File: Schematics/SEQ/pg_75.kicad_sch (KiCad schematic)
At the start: 16 parts, among them U7601 93S48, U7602 93S48, U7603 93S48, U7604 93S48, U7605 F244, U7606 F04, U7607 F02, U7608 F00, U7609 F02, U7610 F51, U7611 F74, U7612 F74, U7613 F74, U7614 F04, U7615 F02, U7616 F51

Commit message: Much work on SEQ
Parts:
- removed U7612, U7613: F74, symbol r1000:F74
- U7611: value F74 -> F175; symbol r1000:F74 -> r1000:F175; Location G36 -> x99
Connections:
- net LEX_ADR.WCS0: now also U7611.12 (D2)
- net MAYBE_DISPATCH~: now also U7611.3 (Q0~); no longer U7611.6 (Q_)
- net PREDECODE.CLK~: now also U7611.9 (CLK); no longer U7611.3 (CLK)
- net PU: no longer U7611.4 (PR_), U7616.1 (A1), U7616.4 (B1)
- net RES_ADR.SEL1: now also U7611.15 (Q3)
- net at U7609.3 (Q): now also U7611.13 (D3)
- net at U7610.7 (Q): now also U7611.4 (D0); no longer U7611.2 (D)
- net at U7616.2 (A2): now also U7611.2 (Q0), U7616.1 (A1); no longer U7611.5 (Q)
- net at U7615.1 (D0), U7616.5 (B2), U7616.6 (B3): now also U7611.10 (Q2), U7616.4 (B1)
- no-connect marks 6 -> 9
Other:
- moved on the sheet: U7608, U7609, U7610, U7614, U7615, U7616

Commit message: KiCad 6
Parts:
- U7601, U7602, U7603, U7604: value 93S48 -> (none)
- U7605: value F244 -> (none)
- U7606, U7614: value F04 -> (none)
- U7607, U7609, U7615: value F02 -> (none)
- U7608: value F00 -> (none)
- U7610, U7616: value F51 -> (none)
- U7611: value F175 -> (none)

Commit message: Recover from KiCad-6 munging
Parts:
- U7601, U7602, U7603, U7604: value (none) -> 93S48
- U7605: value (none) -> F244
- U7606, U7614: value (none) -> F04
- U7607, U7609, U7615: value (none) -> F02
- U7608: value (none) -> F00
- U7610, U7616: value (none) -> F51
- U7611: value (none) -> F175

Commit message: Snapshot
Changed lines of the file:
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@@
   (bus (pts (xy 353.06 345.44) (xy 353.06 350.52) ) )
   (bus (pts (xy 353.06 350.52) (xy 353.06 355.6) ) )
-  (bus (pts (xy 353.06 355.6) (xy 353.06 360.68) ) )
   (wire (pts (xy 124.46 193.04) (xy 124.46 215.9) ) )
   (wire (pts (xy 124.46 215.9) (xy 134.62 215.9) ) )

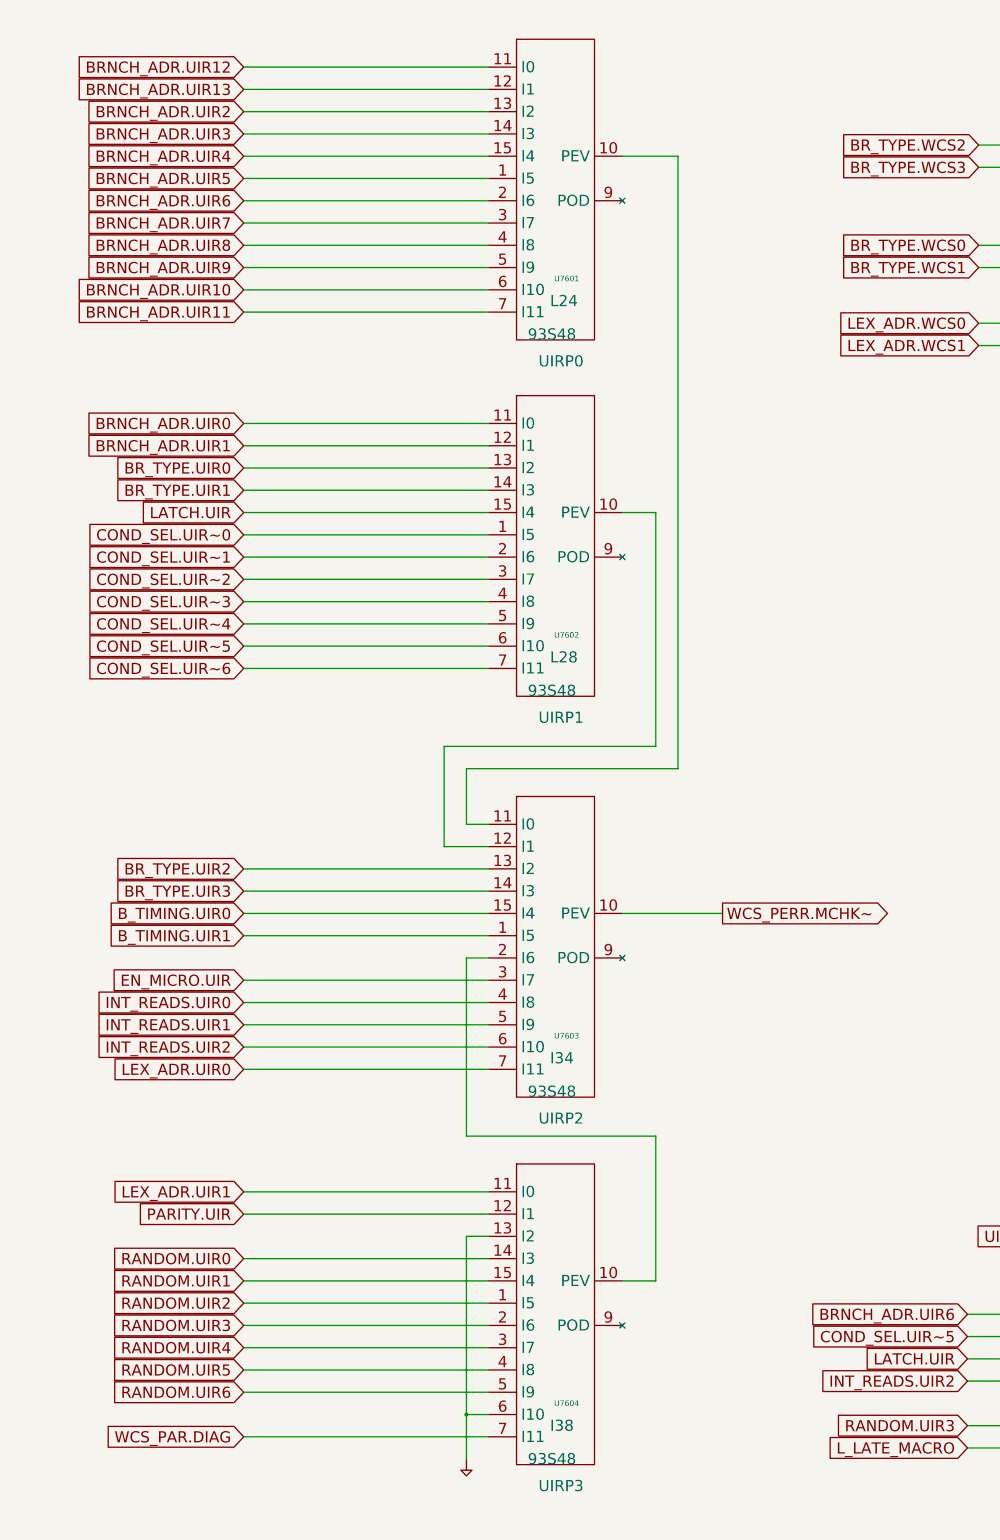
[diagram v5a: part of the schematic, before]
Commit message: Megacom WCS + parity
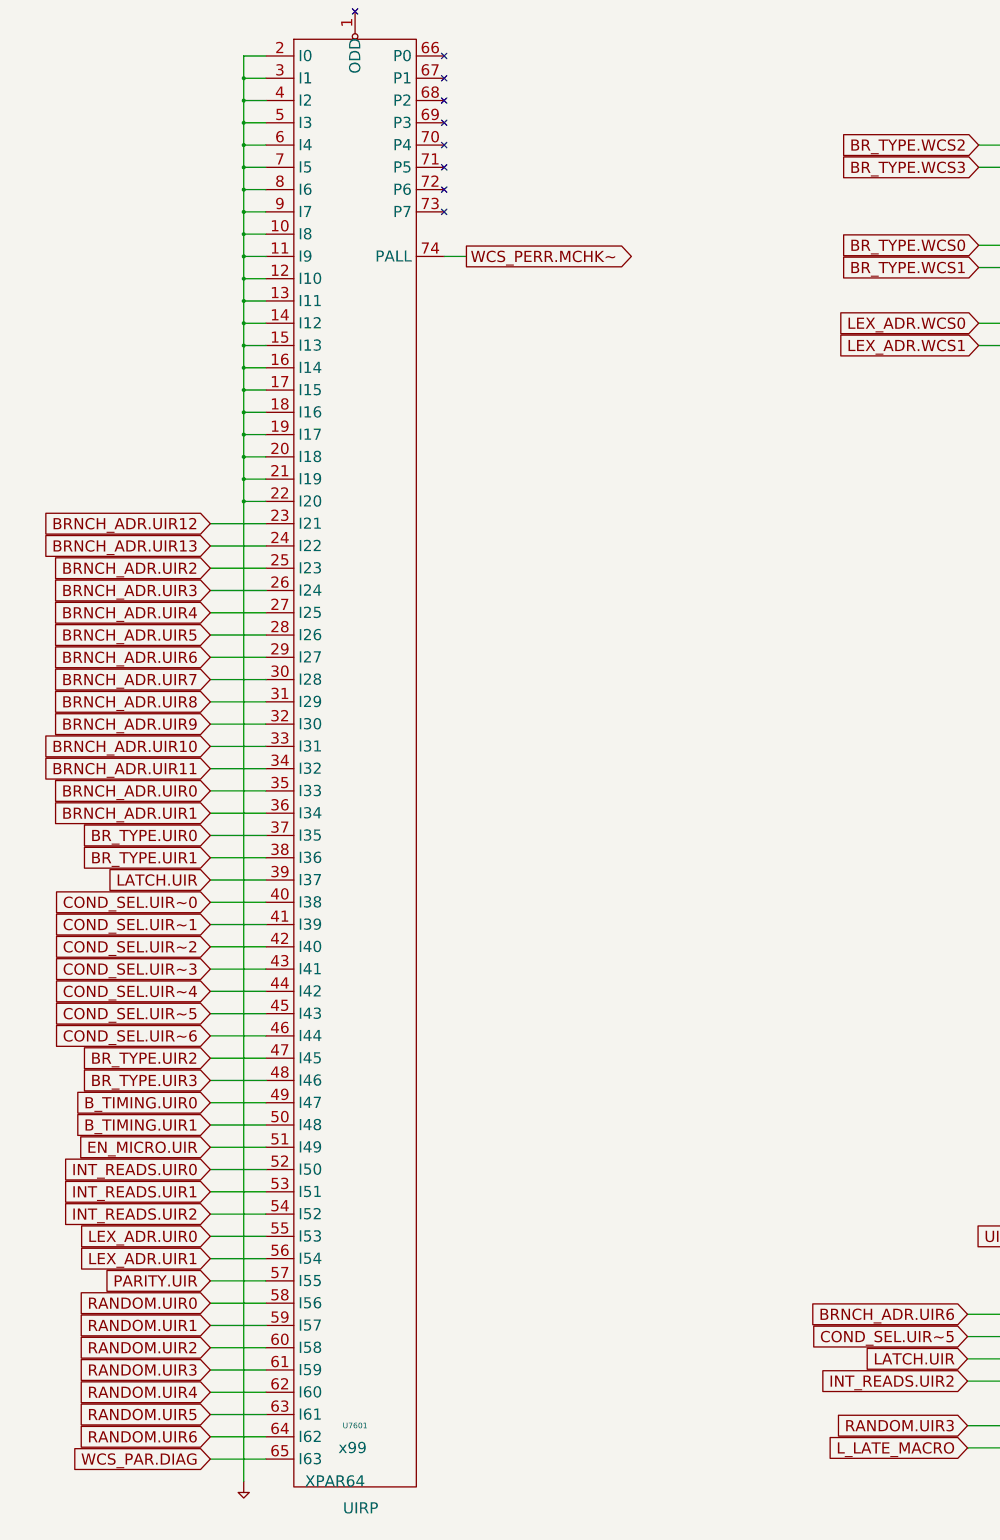
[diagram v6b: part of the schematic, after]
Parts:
- removed U7602, U7603, U7604: 93S48, symbol r1000:93S48
- U7601: value 93S48 -> XPAR64; symbol r1000:93S48 -> r1000:XPAR64; Location L24 -> x99; Name UIRP0 -> UIRP
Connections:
- net BRNCH_ADR.UIR0: now also U7601.35 (I33)
- net BRNCH_ADR.UIR1: now also U7601.36 (I34)
- net BRNCH_ADR.UIR10: now also U7601.33 (I31); no longer U7601.6 (I10)
- net BRNCH_ADR.UIR11: now also U7601.34 (I32); no longer U7601.7 (I11)
- net BRNCH_ADR.UIR12: now also U7601.23 (I21); no longer U7601.11 (I0)
- net BRNCH_ADR.UIR13: now also U7601.24 (I22); no longer U7601.12 (I1)
- net BRNCH_ADR.UIR2: now also U7601.25 (I23); no longer U7601.13 (I2)
- net BRNCH_ADR.UIR3: now also U7601.26 (I24); no longer U7601.14 (I3)
- net BRNCH_ADR.UIR4: now also U7601.27 (I25); no longer U7601.15 (I4)
- net BRNCH_ADR.UIR5: now also U7601.28 (I26); no longer U7601.1 (I5)
- net BRNCH_ADR.UIR6: now also U7601.29 (I27); no longer U7601.2 (I6)
- net BRNCH_ADR.UIR7: now also U7601.30 (I28); no longer U7601.3 (I7)
- net BRNCH_ADR.UIR8: now also U7601.31 (I29); no longer U7601.4 (I8)
- net BRNCH_ADR.UIR9: now also U7601.32 (I30); no longer U7601.5 (I9)
- net BR_TYPE.UIR0: now also U7601.37 (I35)
- net BR_TYPE.UIR1: now also U7601.38 (I36)
- net BR_TYPE.UIR2: now also U7601.47 (I45)
- net BR_TYPE.UIR3: now also U7601.48 (I46)
- net B_TIMING.UIR0: now also U7601.49 (I47)
- net B_TIMING.UIR1: now also U7601.50 (I48)
- net COND_SEL.UIR~0: now also U7601.40 (I38)
- net COND_SEL.UIR~1: now also U7601.41 (I39)
- net COND_SEL.UIR~2: now also U7601.42 (I40)
- net COND_SEL.UIR~3: now also U7601.43 (I41)
- net COND_SEL.UIR~4: now also U7601.44 (I42)
- net COND_SEL.UIR~5: now also U7601.45 (I43)
- net COND_SEL.UIR~6: now also U7601.46 (I44)
- net EN_MICRO.UIR: now also U7601.51 (I49)
- net INT_READS.UIR0: now also U7601.52 (I50)
- net INT_READS.UIR1: now also U7601.53 (I51)
- net INT_READS.UIR2: now also U7601.54 (I52)
- net LATCH.UIR: now also U7601.39 (I37)
- net LEX_ADR.UIR0: now also U7601.55 (I53)
- net LEX_ADR.UIR1: now also U7601.56 (I54)
- net PARITY.UIR: now also U7601.57 (I55)
- net PD: now also U7601.10 (I8), U7601.11 (I9), U7601.12 (I10), U7601.13 (I11), U7601.14 (I12), U7601.15 (I13), U7601.16 (I14), U7601.17 (I15), U7601.18 (I16), U7601.19 (I17), U7601.2 (I0), U7601.20 (I18), U7601.21 (I19), U7601.22 (I20), U7601.3 (I1), U7601.4 (I2), U7601.5 (I3), U7601.6 (I4), U7601.7 (I5), U7601.8 (I6), U7601.9 (I7)
- net RANDOM.UIR0: now also U7601.58 (I56)
- net RANDOM.UIR1: now also U7601.59 (I57)
- net RANDOM.UIR2: now also U7601.60 (I58)
- net RANDOM.UIR3: now also U7601.61 (I59)
- net RANDOM.UIR4: now also U7601.62 (I60)
- net RANDOM.UIR5: now also U7601.63 (I61)
- net RANDOM.UIR6: now also U7601.64 (I62)
- net WCS_PAR.DIAG: now also U7601.65 (I63)
- net WCS_PERR.MCHK~: now also U7601.74 (PALL)
- no-connect marks 9 -> 14

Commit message: Fix polarity of unused part of driven FIU bus.
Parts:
- removed U7601: XPAR64, symbol r1000:XPAR64
- removed U7605: F244, symbol r1000:F244
- removed U7606, U7614: F04, symbol r1000:F04
- removed U7607, U7609, U7615: F02, symbol r1000:F02
- removed U7608: F00, symbol r1000:F00
- removed U7610, U7616: F51, symbol r1000:F51
- removed U7611: F175, symbol r1000:F175
- added U (x2): (no value), symbol r1000:F04
- added U (x3): (no value), symbol r1000:F02
- added U: (no value), symbol r1000:F244
- added U: (no value), symbol r1000:XPAR64
- added U (x2): (no value), symbol r1000:F51
- added U: (no value), symbol r1000:F00
- added U: (no value), symbol r1000:F175
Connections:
- net BRNCH_ADR.UIR0: now also U.35 (I33)
- net BRNCH_ADR.UIR1: now also U.36 (I34)
- net BRNCH_ADR.UIR10: now also U.33 (I31)
- net BRNCH_ADR.UIR11: now also U.34 (I32)
- net BRNCH_ADR.UIR12: now also U.23 (I21)
- net BRNCH_ADR.UIR13: now also U.24 (I22)
- net BRNCH_ADR.UIR2: now also U.25 (I23)
- net BRNCH_ADR.UIR3: now also U.26 (I24)
- net BRNCH_ADR.UIR4: now also U.27 (I25)
- net BRNCH_ADR.UIR5: now also U.28 (I26)
- net BRNCH_ADR.UIR6: now also U.2 (I0), U.29 (I27)
- net BRNCH_ADR.UIR7: now also U.30 (I28)
- net BRNCH_ADR.UIR8: now also U.31 (I29)
- net BRNCH_ADR.UIR9: now also U.32 (I30)
- net BR_TYPE.UIR0: now also U.37 (I35)
- net BR_TYPE.UIR1: now also U.38 (I36)
- net BR_TYPE.UIR2: now also U.47 (I45)
- net BR_TYPE.UIR3: now also U.48 (I46)
- net BR_TYPE.WCS0: now also U.1 (D0)
- net BR_TYPE.WCS1: now also U.2 (D1)
- net BR_TYPE.WCS2: now also U.1 (A1)
- net BR_TYPE.WCS3: now also U.2 (A2)
- net B_TIMING.UIR0: now also U.49 (I47)
- net B_TIMING.UIR1: now also U.50 (I48)
- net COND_SEL.UIR~0: now also U.40 (I38)
- net COND_SEL.UIR~1: now also U.41 (I39)
- net COND_SEL.UIR~2: now also U.42 (I40)
- net COND_SEL.UIR~3: now also U.43 (I41)
- net COND_SEL.UIR~4: now also U.44 (I42)
- net COND_SEL.UIR~5: now also U.4 (I1), U.45 (I43)
- net COND_SEL.UIR~6: now also U.46 (I44)
- net DIAG.D0: now also U.18 (Y0)
- net DIAG.D1: now also U.16 (Y1)
- net DIAG.D2: now also U.14 (Y2)
- net DIAG.D3: now also U.12 (Y3)
- net DIAG.D4: now also U.9 (Y4)
- net DIAG.D5: now also U.7 (Y5)
- net DIAG.D6: now also U.5 (Y6)
- net DIAG.D7: now also U.3 (Y7)
- net DISP~0: now also U.1 (D0)
- net EN_MICRO.UIR: now also U.51 (I49)
- net INT_READS.UIR0: now also U.52 (I50)
- net INT_READS.UIR1: now also U.53 (I51)
- net INT_READS.UIR2: now also U.54 (I52), U.8 (I3)
- net LATCH.UIR: now also U.39 (I37), U.6 (I2)
- net LATE_MACRO: now also U.1 (D0)
- net LEX_ADR.UIR0: now also U.55 (I53)
- net LEX_ADR.UIR1: now also U.56 (I54)
- net LEX_ADR.WCS0: now also U.1 (D0), U.12 (D2)
- net LEX_ADR.WCS1: now also U.2 (D1)
- net LEX_IS_INCOMING: now also U.3 (Q)
- net L_LATE_MACRO: now also U.15 (I6)
- net MAYBE_DISPATCH~: now also U.3 (Q0~)
- net NEXT_LATE_MACRO: now also U.3 (Q)
- net PARITY.UIR: now also U.57 (I55)
- net PD: now also U.10 (I8), U.11 (I4), U.11 (I9), U.12 (I10), U.13 (I11), U.14 (I12), U.15 (I13), U.16 (I14), U.17 (I15), U.17 (I7), U.18 (I16), U.19 (I17), U.2 (I0), U.20 (I18), U.21 (I19), U.22 (I20), U.3 (I1), U.4 (I2), U.5 (I3), U.6 (I4), U.7 (I5), U.8 (I6), U.9 (I7)
- net PREDECODE.CLK~: now also U.9 (CLK)
- net PU: now also U.1 (CLR), U.3 (A3)
- net RANDOM.UIR0: now also U.58 (I56)
- net RANDOM.UIR1: now also U.59 (I57)
- net RANDOM.UIR2: now also U.60 (I58)
- net RANDOM.UIR3: now also U.13 (I5), U.61 (I59)
- net RANDOM.UIR4: now also U.62 (I60)
- net RANDOM.UIR5: now also U.63 (I61)
- net RANDOM.UIR6: now also U.64 (I62)
- net RES_ADR.SEL0: now also U.7 (Q)
- net RES_ADR.SEL1: now also U.15 (Q3), U.2 (D1)
- net STATE.CLKEN~: now also U.2 (D1)
- net UIR_SCAN.OE~: now also U.1 (OE0), U.19 (OE1)
- net WCS_PAR.DIAG: now also U.65 (I63)
- net WCS_PERR.MCHK~: now also U.74 (PALL)
- new net: U.1 (D0), U.2 (Q)
- new net: U.3 (Q), U.4 (B1), U.5 (B2), U.6 (B3)
- new net: U.4 (D0), U.7 (Q)
- new net: U.1 (A1), U.2 (A2), U.2 (Q0)
- new net: U.2 (Q), U.3 (A3)
- new net: U.1 (D0), U.10 (Q2), U.4 (B1), U.5 (B2), U.6 (B3)
- new net: U.13 (D3), U.3 (Q)

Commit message: Fix WCS parity
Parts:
- removed U: (no value), symbol r1000:F244
- removed U: (no value), symbol r1000:XPAR64
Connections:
- no-connect marks 14 -> 5
